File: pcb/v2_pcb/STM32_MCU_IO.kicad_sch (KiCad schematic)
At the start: 1 part, among them U1 STM32N657X0H3Q

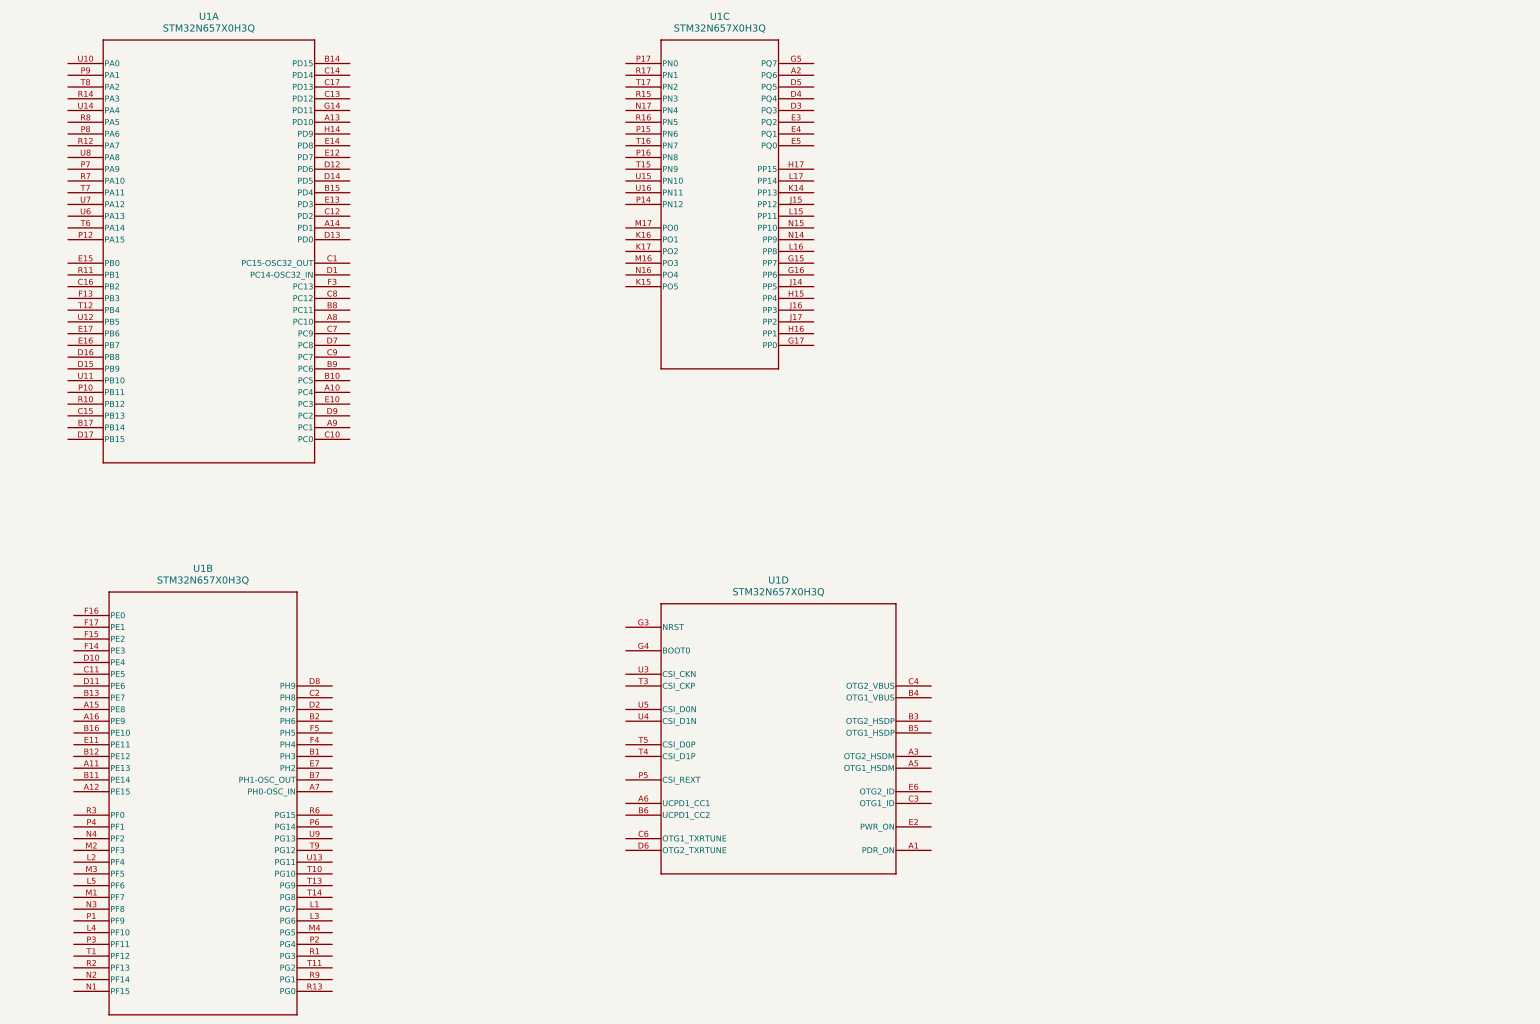
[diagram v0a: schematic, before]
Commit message: add io pinouts
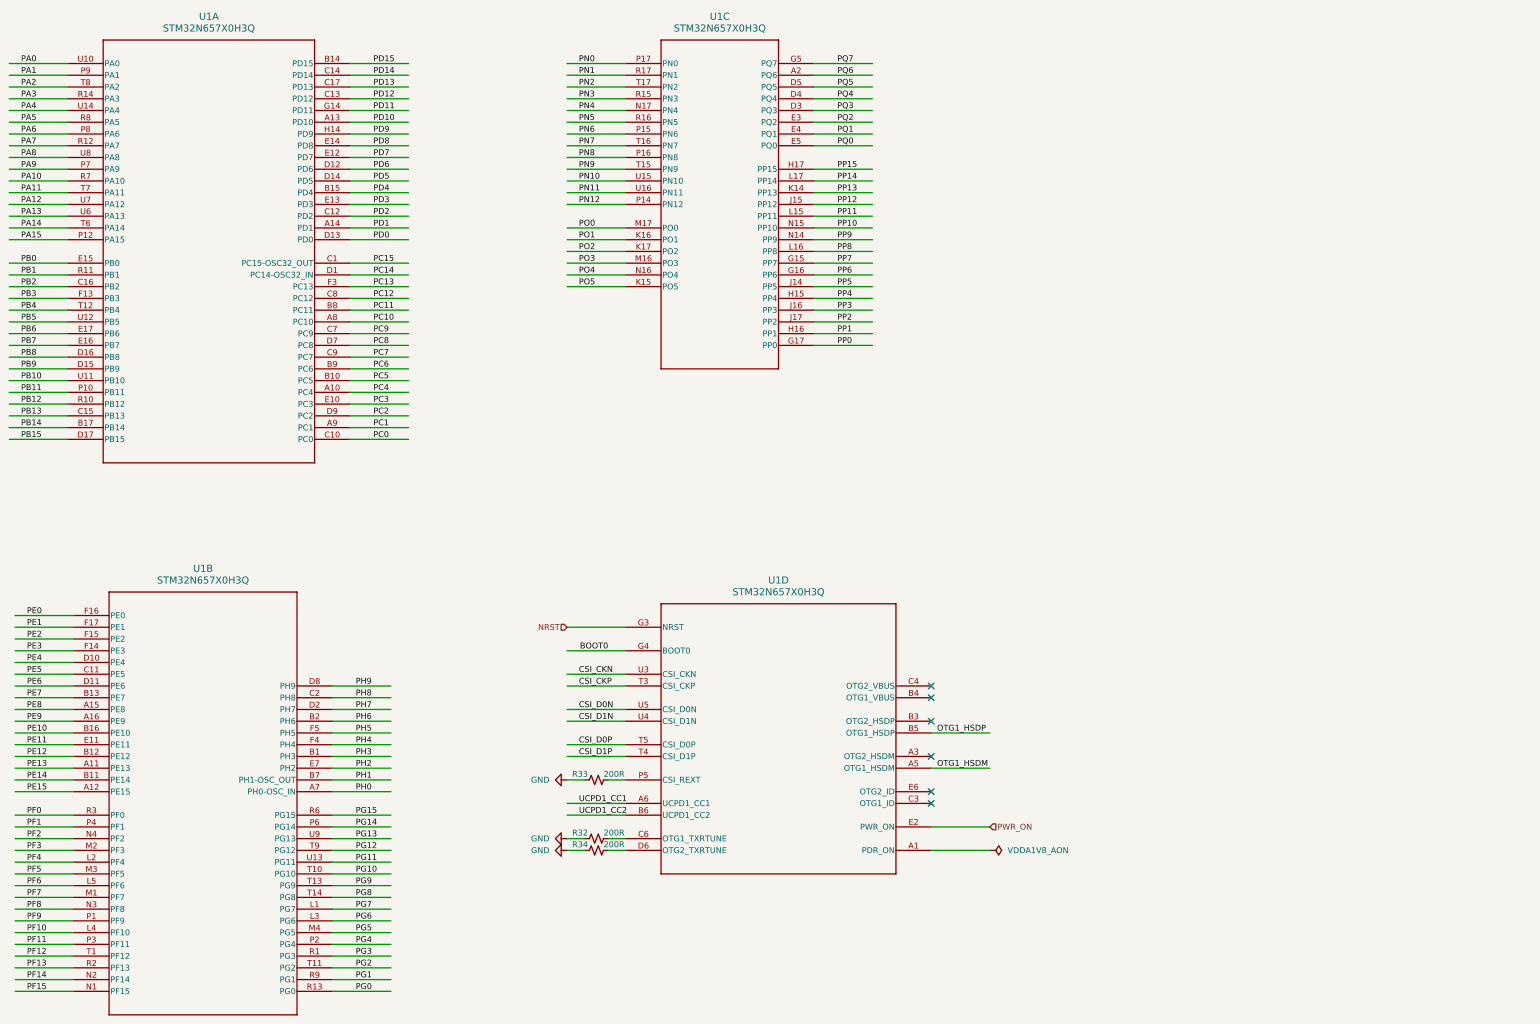
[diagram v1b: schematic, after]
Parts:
- added R32, R33, R34: 200R, symbol Device:R_Small_US
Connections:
- net PE13: now reaches U1.A11 (PE13)
- net PE15: now reaches U1.A12 (PE15)
- net PE8: now reaches U1.A15 (PE8)
- net PE9: now reaches U1.A16 (PE9)
- net PH0: now reaches U1.A7 (PH0-OSC_IN)
- net PH3: now reaches U1.B1 (PH3)
- net PE14: now reaches U1.B11 (PE14)
- net PE12: now reaches U1.B12 (PE12)
- net PE7: now reaches U1.B13 (PE7)
- net PE10: now reaches U1.B16 (PE10)
- net PH6: now reaches U1.B2 (PH6)
- net PH1: now reaches U1.B7 (PH1-OSC_OUT)
- net PE5: now reaches U1.C11 (PE5)
- net PH8: now reaches U1.C2 (PH8)
- net PE4: now reaches U1.D10 (PE4)
- net PE6: now reaches U1.D11 (PE6)
- net PH7: now reaches U1.D2 (PH7)
- net PH9: now reaches U1.D8 (PH9)
- net PE11: now reaches U1.E11 (PE11)
- net PH2: now reaches U1.E7 (PH2)
- net PE3: now reaches U1.F14 (PE3)
- net PE2: now reaches U1.F15 (PE2)
- net PE0: now reaches U1.F16 (PE0)
- net PE1: now reaches U1.F17 (PE1)
- net PH4: now reaches U1.F4 (PH4)
- net PH5: now reaches U1.F5 (PH5)
- net PG7: now reaches U1.L1 (PG7)
- net PF4: now reaches U1.L2 (PF4)
- net PG6: now reaches U1.L3 (PG6)
- net PF10: now reaches U1.L4 (PF10)
- net PF6: now reaches U1.L5 (PF6)
- net PF7: now reaches U1.M1 (PF7)
- net PF3: now reaches U1.M2 (PF3)
- net PF5: now reaches U1.M3 (PF5)
- net PG5: now reaches U1.M4 (PG5)
- net PF15: now reaches U1.N1 (PF15)
- net PF14: now reaches U1.N2 (PF14)
- net PF8: now reaches U1.N3 (PF8)
- net PF2: now reaches U1.N4 (PF2)
- net PF9: now reaches U1.P1 (PF9)
- net PG4: now reaches U1.P2 (PG4)
- net PF11: now reaches U1.P3 (PF11)
- net PF1: now reaches U1.P4 (PF1)
- net PG14: now reaches U1.P6 (PG14)
- net PG3: now reaches U1.R1 (PG3)
- net PG0: now reaches U1.R13 (PG0)
- net PF13: now reaches U1.R2 (PF13)
- net PF0: now reaches U1.R3 (PF0)
- net PG15: now reaches U1.R6 (PG15)
- net PG1: now reaches U1.R9 (PG1)
- net PF12: now reaches U1.T1 (PF12)
- net PG10: now reaches U1.T10 (PG10)
- net PG2: now reaches U1.T11 (PG2)
- net PG9: now reaches U1.T13 (PG9)
- net PG8: now reaches U1.T14 (PG8)
- net PG12: now reaches U1.T9 (PG12)
- net PG11: now reaches U1.U13 (PG11)
- net PG13: now reaches U1.U9 (PG13)
- net PQ6: now reaches U1.A2 (PQ6)
- net PQ3: now reaches U1.D3 (PQ3)
- net PQ4: now reaches U1.D4 (PQ4)
- net PQ5: now reaches U1.D5 (PQ5)
- net PQ2: now reaches U1.E3 (PQ2)
- net PQ1: now reaches U1.E4 (PQ1)
- net PQ0: now reaches U1.E5 (PQ0)
- net PP7: now reaches U1.G15 (PP7)
- net PP6: now reaches U1.G16 (PP6)
- net PP0: now reaches U1.G17 (PP0)
- net PQ7: now reaches U1.G5 (PQ7)
- net PP4: now reaches U1.H15 (PP4)
- net PP1: now reaches U1.H16 (PP1)
- net PP15: now reaches U1.H17 (PP15)
- net PP5: now reaches U1.J14 (PP5)
- net PP12: now reaches U1.J15 (PP12)
- net PP3: now reaches U1.J16 (PP3)
- net PP2: now reaches U1.J17 (PP2)
- net PP13: now reaches U1.K14 (PP13)
- net PO5: now reaches U1.K15 (PO5)
- net PO1: now reaches U1.K16 (PO1)
- net PO2: now reaches U1.K17 (PO2)
- net PP11: now reaches U1.L15 (PP11)
- net PP8: now reaches U1.L16 (PP8)
- net PP14: now reaches U1.L17 (PP14)
- net PO3: now reaches U1.M16 (PO3)
- net PO0: now reaches U1.M17 (PO0)
- net PP9: now reaches U1.N14 (PP9)
- net PP10: now reaches U1.N15 (PP10)
- net PO4: now reaches U1.N16 (PO4)
- net PN4: now reaches U1.N17 (PN4)
- net PN12: now reaches U1.P14 (PN12)
- net PN6: now reaches U1.P15 (PN6)
- net PN8: now reaches U1.P16 (PN8)
- net PN0: now reaches U1.P17 (PN0)
- net PN3: now reaches U1.R15 (PN3)
- net PN5: now reaches U1.R16 (PN5)
- net PN1: now reaches U1.R17 (PN1)
- net PN9: now reaches U1.T15 (PN9)
- net PN7: now reaches U1.T16 (PN7)
- net PN2: now reaches U1.T17 (PN2)
- net PN10: now reaches U1.U15 (PN10)
- net PN11: now reaches U1.U16 (PN11)
- net OTG1_HSDM: now reaches U1.A5 (OTG1_HSDM)
- net UCPD1_CC1: now reaches U1.A6 (UCPD1_CC1)
- net OTG1_HSDP: now reaches U1.B5 (OTG1_HSDP)
- net UCPD1_CC2: now reaches U1.B6 (UCPD1_CC2)
- net at U1.C6 (OTG1_TXRTUNE): now also R32.2
- net at U1.D6 (OTG2_TXRTUNE): now also R34.2
- net PWR_ON: now reaches U1.E2 (PWR_ON)
- net NRST: now reaches U1.G3 (NRST)
- net BOOT0: now reaches U1.G4 (BOOT0)
- net at U1.P5 (CSI_REXT): now also R33.2
- net CSI_CKP: now reaches U1.T3 (CSI_CKP)
- net CSI_D1P: now reaches U1.T4 (CSI_D1P)
- net CSI_D0P: now reaches U1.T5 (CSI_D0P)
- net CSI_CKN: now reaches U1.U3 (CSI_CKN)
- net CSI_D1N: now reaches U1.U4 (CSI_D1N)
- net CSI_D0N: now reaches U1.U5 (CSI_D0N)
- net PC4: now reaches U1.A10 (PC4)
- net PD10: now reaches U1.A13 (PD10)
- net PD1: now reaches U1.A14 (PD1)
- net PC10: now reaches U1.A8 (PC10)
- net PC1: now reaches U1.A9 (PC1)
- net PC5: now reaches U1.B10 (PC5)
- net PD15: now reaches U1.B14 (PD15)
- net PD4: now reaches U1.B15 (PD4)
- net PB14: now reaches U1.B17 (PB14)
- net PC11: now reaches U1.B8 (PC11)
- net PC6: now reaches U1.B9 (PC6)
- net PC15: now reaches U1.C1 (PC15-OSC32_OUT)
- net PC0: now reaches U1.C10 (PC0)
- net PD2: now reaches U1.C12 (PD2)
- net PD12: now reaches U1.C13 (PD12)
- net PD14: now reaches U1.C14 (PD14)
- net PB13: now reaches U1.C15 (PB13)
- net PB2: now reaches U1.C16 (PB2)
- net PD13: now reaches U1.C17 (PD13)
- net PC9: now reaches U1.C7 (PC9)
- net PC12: now reaches U1.C8 (PC12)
- net PC7: now reaches U1.C9 (PC7)
- net PC14: now reaches U1.D1 (PC14-OSC32_IN)
- net PD6: now reaches U1.D12 (PD6)
- net PD0: now reaches U1.D13 (PD0)
- net PD5: now reaches U1.D14 (PD5)
- net PB9: now reaches U1.D15 (PB9)
- net PB8: now reaches U1.D16 (PB8)
- net PB15: now reaches U1.D17 (PB15)
- net PC8: now reaches U1.D7 (PC8)
- net PC2: now reaches U1.D9 (PC2)
- net PC3: now reaches U1.E10 (PC3)
- net PD7: now reaches U1.E12 (PD7)
- net PD3: now reaches U1.E13 (PD3)
- net PD8: now reaches U1.E14 (PD8)
- net PB0: now reaches U1.E15 (PB0)
- net PB7: now reaches U1.E16 (PB7)
- net PB6: now reaches U1.E17 (PB6)
- net PB3: now reaches U1.F13 (PB3)
- net PC13: now reaches U1.F3 (PC13)
- net PD11: now reaches U1.G14 (PD11)
- net PD9: now reaches U1.H14 (PD9)
- net PB11: now reaches U1.P10 (PB11)
- net PA15: now reaches U1.P12 (PA15)
- net PA9: now reaches U1.P7 (PA9)
- net PA6: now reaches U1.P8 (PA6)
- net PA1: now reaches U1.P9 (PA1)
- net PB12: now reaches U1.R10 (PB12)
- net PB1: now reaches U1.R11 (PB1)
- net PA7: now reaches U1.R12 (PA7)
- net PA3: now reaches U1.R14 (PA3)
- net PA10: now reaches U1.R7 (PA10)
- net PA5: now reaches U1.R8 (PA5)
- net PB4: now reaches U1.T12 (PB4)
- net PA14: now reaches U1.T6 (PA14)
- net PA11: now reaches U1.T7 (PA11)
- net PA2: now reaches U1.T8 (PA2)
- net PA0: now reaches U1.U10 (PA0)
- net PB10: now reaches U1.U11 (PB10)
- net PB5: now reaches U1.U12 (PB5)
- net PA4: now reaches U1.U14 (PA4)
- net PA13: now reaches U1.U6 (PA13)
- net PA12: now reaches U1.U7 (PA12)
- net PA8: now reaches U1.U8 (PA8)
- new net GND: R32.1, R33.1, R34.1
- no-connect marks 0 -> 6

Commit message: add ram
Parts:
- added R44, R45, R46, R47, R48, R49, R50, R51, R53, R54, R55, R56, R57, R58, R59, R60, R61, R62, R63, R64: Resistor, Library:R0402, symbol Device:R_Small_US
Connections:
- net PO0: now also R62.2
- net PO2: now also R56.2
- net PO3: now also R59.2
- net PO4: now also R58.2
- net PP0: now also R55.2
- net PP1: now also R47.2
- net PP10: now also R50.2
- net PP11: now also R49.2
- net PP12: now also R60.2
- net PP13: now also R48.2
- net PP14: now also R46.2
- net PP15: now also R61.2
- net PP2: now also R45.2
- net PP3: now also R57.2
- net PP4: now also R44.2
- net PP5: now also R54.2
- net PP6: now also R53.2
- net PP7: now also R51.2
- net PP8: now also R64.2
- net PP9: now also R63.2

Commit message: add debug to pcb
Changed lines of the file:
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@@
 	)
 	(bus_entry
+		(at 316.23 144.78)
+		(size 2.54 2.54)
+		(stroke
+			(width 0)
+			(type default)
+		)
+	)
+	(bus_entry
 		(at 320.04 78.74)
 		(size 2.54 2.54)
@@
 	)
 	(bus_entry
+		(at 316.23 139.7)
+		(size 2.54 2.54)
+		(stroke
+			(width 0)
+			(type default)
+		)
+	)
+	(bus_entry
 		(at 320.04 114.3)
 		(size 2.54 2.54)
@@
 	)
 	(bus_entry
+		(at 316.23 142.24)
+		(size 2.54 2.54)
+		(stroke
+			(width 0)
+			(type default)
+		)
+	)
+	(bus_entry
 		(at 320.04 91.44)
 		(size 2.54 2.54)
@@
 		)
 	)
+	(bus
+		(pts
+			(xy 318.77 148.59) (xy 318.77 139.7)
+		)
+		(stroke
+			(width 0)
+			(type default)
+		)
+	)
 	(wire
 		(pts
@@
 	(wire
 		(pts
+			(xy 300.99 139.7) (xy 316.23 139.7)
+		)
+		(stroke
+			(width 0)
+			(type default)
+		)
+	)
+	(wire
+		(pts
 			(xy 146.05 48.26) (xy 158.75 48.26)
 		)
@@
 	(wire
 		(pts
+			(xy 300.99 144.78) (xy 316.23 144.78)
+		)
+		(stroke
+			(width 0)
+			(type default)
+		)
+	)
+	(wire
+		(pts
 			(xy 193.04 58.42) (xy 205.74 58.42)
 		)
@@
 	(wire
 		(pts
+			(xy 300.99 142.24) (xy 316.23 142.24)
+		)
+		(stroke
+			(width 0)
+			(type default)
+		)
+	)
+	(wire
+		(pts
 			(xy 73.66 205.74) (xy 86.36 205.74)
 		)
@@
 		)
 	)
+	(label "SWCLK"
+		(at 316.23 139.7 180)
+		(effects
+			(font
+				(size 1.27 1.27)
+			)
+			(justify right bottom)
+		)
+	)
 	(label "PD12"
 		(at 158.75 50.8 180)
@@
 	)
 	(label "PA13"
+		(at 300.99 142.24 0)
+		(effects
+			(font
+				(size 1.27 1.27)
+			)
+			(justify left bottom)
+		)
+	)
+	(label "PA13"
 		(at 72.39 76.2 0)
 		(effects
@@
 		)
 	)
+	(label "DEBUGPROBE{SWCLK SWDIO SWO}"
+		(at 318.77 139.7 0)
+		(effects
+			(font
+				(size 1.27 1.27)
+			)
+			(justify left bottom)
+		)
+	)
 	(label "PB12"
 		(at 72.39 116.84 0)
@@
 		)
 	)
+	(label "PB3"
+		(at 300.99 144.78 0)
+		(effects
+			(font
+				(size 1.27 1.27)
+			)
+			(justify left bottom)
+		)
+	)
 	(label "CSI_D0N"
 		(at 193.0129 182.88 0)
@@
 		)
 	)
+	(label "SWO"
+		(at 316.23 144.78 180)
+		(effects
+			(font
+				(size 1.27 1.27)
+			)
+			(justify right bottom)
+		)
+	)
 	(label "PP8"
 		(at 259.08 83.82 180)
@@
 		)
 	)
+	(label "PA14"
+		(at 300.99 139.7 0)
+		(effects
+			(font
+				(size 1.27 1.27)
+			)
+			(justify left bottom)
+		)
+	)
 	(label "PD2"
 		(at 158.75 76.2 180)
@@
 		)
 	)
+	(label "SWDIO"
+		(at 316.23 142.24 180)
+		(effects
+			(font
+				(size 1.27 1.27)
+			)
+			(justify right bottom)
+		)
+	)
 	(label "PC8"
 		(at 158.75 104.14 180)
@@
 		(effects
 			(font
+				(size 1.27 1.27)
+			)
+			(justify left)
+		)
+	)
+	(hierarchical_label "DEBUGPROBE"
+		(shape input)
+		(at 318.77 148.59 0)
+		(effects
+			(font
